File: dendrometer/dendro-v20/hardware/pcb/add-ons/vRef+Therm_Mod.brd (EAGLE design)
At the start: 10.2 x 15.7 mm, 9 parts, among them J1 MF-CON-2.54mm-01x03, J2 CON_01X01LUX, J4 MF-CON-2.54mm-01x03, U1 LM4040-SOT-23-3

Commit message: forgot to save
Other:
- board size 10.2 x 15.7 mm -> 8.9 x 15.2 mm
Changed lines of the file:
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@@
 <board>
 <plain>
-<wire x1="0" y1="0" x2="10.16" y2="0" width="0" layer="20"/>
-<wire x1="10.16" y1="0" x2="10.16" y2="15.24" width="0" layer="20"/>
-<wire x1="10.16" y1="15.24" x2="0" y2="15.24" width="0" layer="20"/>
+<wire x1="0" y1="0" x2="8.89" y2="0" width="0" layer="20"/>
+<wire x1="8.89" y1="0" x2="8.89" y2="15.24" width="0" layer="20"/>
+<wire x1="8.89" y1="15.24" x2="0" y2="15.24" width="0" layer="20"/>
 <wire x1="0" y1="15.24" x2="0" y2="0" width="0" layer="20"/>
 <wire x1="1.27" y1="0.635" x2="3.81" y2="0.635" width="0.3048" layer="46"/>
@@
 <wire x1="8.128" y1="3.429" x2="8.128" y2="5.842" width="0.3048" layer="46"/>
 <wire x1="8.128" y1="5.842" x2="8.763" y2="6.477" width="0.3048" layer="46"/>
-<wire x1="6.223" y1="13.208" x2="6.223" y2="15.621" width="0.3048" layer="46"/>
-<wire x1="1.397" y1="15.748" x2="1.397" y2="13.081" width="0.3048" layer="46"/>
 <wire x1="1.397" y1="13.081" x2="1.905" y2="12.827" width="0.3048" layer="46"/>
 <wire x1="1.905" y1="12.827" x2="2.921" y2="12.827" width="0.3048" layer="46"/>
@@
 <wire x1="7.112" y1="5.969" x2="8.001" y2="6.858" width="0.3048" layer="46"/>
 <wire x1="4.572" y1="12.319" x2="3.937" y2="12.954" width="0.3048" layer="46"/>
-<wire x1="3.937" y1="12.954" x2="3.937" y2="15.621" width="0.3048" layer="46"/>
 <wire x1="1.27" y1="0.635" x2="1.27" y2="2.159" width="0.3048" layer="46"/>
 <wire x1="1.27" y1="2.159" x2="2.032" y2="2.921" width="0.3048" layer="46"/>
@@
 <wire x1="6.858" y1="11.938" x2="6.477" y2="12.319" width="0.3048" layer="46"/>
 <wire x1="6.477" y1="12.319" x2="6.477" y2="12.954" width="0.3048" layer="46"/>
-<wire x1="6.477" y1="12.954" x2="6.223" y2="13.208" width="0.3048" layer="46"/>
+<wire x1="6.477" y1="12.954" x2="6.35" y2="13.081" width="0.3048" layer="46"/>
 <wire x1="4.191" y1="11.557" x2="5.207" y2="11.557" width="0.3048" layer="46"/>
 <wire x1="5.207" y1="11.557" x2="7.239" y2="9.525" width="0.3048" layer="46"/>
@@
 <wire x1="3.429" y1="2.921" x2="3.429" y2="4.699" width="0.3048" layer="46"/>
 <wire x1="3.429" y1="4.699" x2="3.937" y2="4.699" width="0.3048" layer="46"/>
+<wire x1="1.397" y1="13.081" x2="1.397" y2="14.605" width="0.3048" layer="46"/>
+<wire x1="1.397" y1="14.605" x2="3.937" y2="14.605" width="0.3048" layer="46"/>
+<wire x1="3.937" y1="14.605" x2="6.223" y2="14.605" width="0.3048" layer="46"/>
+<wire x1="6.223" y1="14.605" x2="6.35" y2="14.478" width="0.3048" layer="46"/>
+<wire x1="6.35" y1="14.478" x2="6.35" y2="13.081" width="0.3048" layer="46"/>
+<wire x1="3.937" y1="12.954" x2="3.937" y2="14.605" width="0.3048" layer="46"/>
 </plain>
 <attributes>

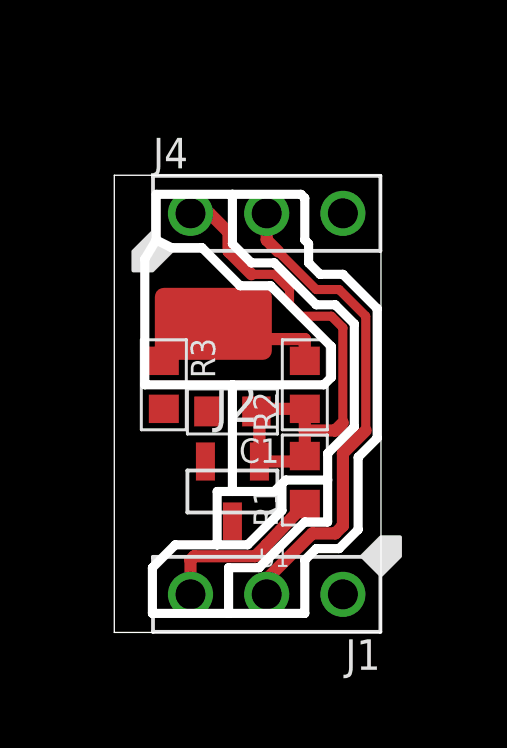
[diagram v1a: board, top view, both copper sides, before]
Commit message: making add-on boards for dendro upgrades)
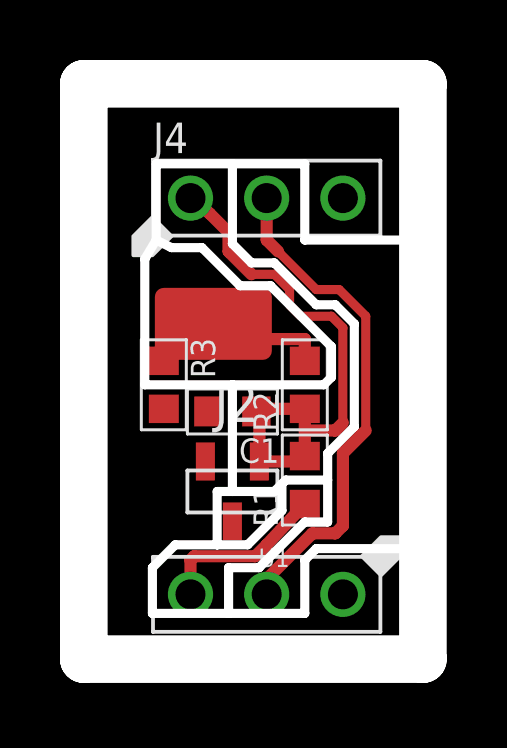
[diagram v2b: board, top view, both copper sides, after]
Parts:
- moved FRAME1 3.59 mm to (6.35, 19.1)
- moved J4 0.51 mm to (5.08, 14.5)
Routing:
- net SENSE: track 16.3 -> 16.8 mm
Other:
- board size 8.9 x 15.2 mm -> 11.3 x 19.2 mm
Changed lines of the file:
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@@
 <?xml version="1.0" encoding="utf-8"?>
 <!DOCTYPE eagle SYSTEM "eagle.dtd">
-<eagle version="8.0.0">
+<eagle version="8.0.1">
 <drawing>
 <settings>
@@
 <layer number="19" name="Unrouted" color="6" fill="1" visible="yes" active="yes"/>
 <layer number="20" name="Dimension" color="15" fill="1" visible="yes" active="yes"/>
-<layer number="21" name="tPlace" color="7" fill="1" visible="yes" active="yes"/>
-<layer number="22" name="bPlace" color="7" fill="1" visible="yes" active="yes"/>
+<layer number="21" name="tPlace" color="16" fill="1" visible="yes" active="yes"/>
+<layer number="22" name="bPlace" color="5" fill="1" visible="yes" active="yes"/>
 <layer number="23" name="tOrigins" color="15" fill="1" visible="yes" active="yes"/>
 <layer number="24" name="bOrigins" color="15" fill="1" visible="yes" active="yes"/>
@@
 <layer number="49" name="Reference" color="7" fill="1" visible="yes" active="yes"/>
 <layer number="50" name="dxf" color="7" fill="1" visible="no" active="no"/>
-<layer number="51" name="tDocu" color="7" fill="1" visible="yes" active="yes"/>
+<layer number="51" name="tDocu" color="6" fill="1" visible="yes" active="yes"/>
 <layer number="52" name="bDocu" color="7" fill="1" visible="no" active="yes"/>
 <layer number="53" name="tGND_GNDA" color="7" fill="9" visible="no" active="no"/>
@@
 <board>
 <plain>
-<wire x1="0" y1="0" x2="8.89" y2="0" width="0" layer="20"/>
-<wire x1="8.89" y1="0" x2="8.89" y2="15.24" width="0" layer="20"/>
-<wire x1="8.89" y1="15.24" x2="0" y2="15.24" width="0" layer="20"/>
-<wire x1="0" y1="15.24" x2="0" y2="0" width="0" layer="20"/>
+<wire x1="-1.016" y1="-0.889" x2="10.287" y2="-0.889" width="1.5875" layer="20"/>
+<wire x1="10.287" y1="-0.889" x2="10.287" y2="18.288" width="1.5875" layer="20"/>
+<wire x1="10.287" y1="18.288" x2="-1.016" y2="18.288" width="1.5875" layer="20"/>
+<wire x1="-1.016" y1="18.288" x2="-1.016" y2="-0.889" width="1.5875" layer="20"/>
 <wire x1="1.27" y1="0.635" x2="3.81" y2="0.635" width="0.3048" layer="46"/>
 <wire x1="3.81" y1="0.635" x2="6.35" y2="0.635" width="0.3048" layer="46"/>
 <wire x1="6.35" y1="0.635" x2="6.35" y2="2.413" width="0.3048" layer="46"/>
 <wire x1="6.35" y1="2.413" x2="6.731" y2="2.794" width="0.3048" layer="46"/>
-<wire x1="6.731" y1="2.794" x2="7.493" y2="2.794" width="0.3048" layer="46"/>
-<wire x1="7.493" y1="2.794" x2="8.128" y2="3.429" width="0.3048" layer="46"/>
-<wire x1="8.128" y1="3.429" x2="8.128" y2="5.842" width="0.3048" layer="46"/>
-<wire x1="8.128" y1="5.842" x2="8.763" y2="6.477" width="0.3048" layer="46"/>
+<wire x1="6.731" y1="2.794" x2="9.906" y2="2.794" width="0.3048" layer="46"/>
 <wire x1="1.397" y1="13.081" x2="1.905" y2="12.827" width="0.3048" layer="46"/>
 <wire x1="1.905" y1="12.827" x2="2.921" y2="12.827" width="0.3048" layer="46"/>
@@
 <wire x1="7.366" y1="10.922" x2="8.001" y2="10.287" width="0.3048" layer="46"/>
 <wire x1="8.001" y1="10.287" x2="8.001" y2="6.858" width="0.3048" layer="46"/>
-<wire x1="8.763" y1="6.477" x2="8.763" y2="10.795" width="0.3048" layer="46"/>
-<wire x1="8.763" y1="10.795" x2="7.62" y2="11.938" width="0.3048" layer="46"/>
-<wire x1="7.62" y1="11.938" x2="6.858" y2="11.938" width="0.3048" layer="46"/>
-<wire x1="6.858" y1="11.938" x2="6.477" y2="12.319" width="0.3048" layer="46"/>
-<wire x1="6.477" y1="12.319" x2="6.477" y2="12.954" width="0.3048" layer="46"/>
-<wire x1="6.477" y1="12.954" x2="6.35" y2="13.081" width="0.3048" layer="46"/>
+<wire x1="10.033" y1="13.081" x2="6.35" y2="13.081" width="0.3048" layer="46"/>
 <wire x1="4.191" y1="11.557" x2="5.207" y2="11.557" width="0.3048" layer="46"/>
 <wire x1="5.207" y1="11.557" x2="7.239" y2="9.525" width="0.3048" layer="46"/>
@@
 <wire x1="3.429" y1="2.921" x2="3.429" y2="4.699" width="0.3048" layer="46"/>
 <wire x1="3.429" y1="4.699" x2="3.937" y2="4.699" width="0.3048" layer="46"/>
-<wire x1="1.397" y1="13.081" x2="1.397" y2="14.605" width="0.3048" layer="46"/>
-<wire x1="1.397" y1="14.605" x2="3.937" y2="14.605" width="0.3048" layer="46"/>
-<wire x1="3.937" y1="14.605" x2="6.223" y2="14.605" width="0.3048" layer="46"/>
-<wire x1="6.223" y1="14.605" x2="6.35" y2="14.478" width="0.3048" layer="46"/>
-<wire x1="6.35" y1="14.478" x2="6.35" y2="13.081" width="0.3048" layer="46"/>
-<wire x1="3.937" y1="12.954" x2="3.937" y2="14.605" width="0.3048" layer="46"/>
+<wire x1="1.397" y1="13.081" x2="1.397" y2="15.621" width="0.3048" layer="46"/>
+<wire x1="1.397" y1="15.621" x2="3.937" y2="15.621" width="0.3048" layer="46"/>
+<wire x1="3.937" y1="15.621" x2="6.35" y2="15.621" width="0.3048" layer="46"/>
+<wire x1="6.35" y1="15.621" x2="6.35" y2="13.081" width="0.3048" layer="46"/>
+<wire x1="3.937" y1="12.954" x2="3.937" y2="15.621" width="0.3048" layer="46"/>
 </plain>
 <attributes>
@@
 <attribute name="PARTNO" value="" x="3.937" y="7.366" size="1.778" layer="27" rot="R180" display="off"/>
 </element>
-<element name="FRAME1" library="My_Aesthetics" package="DUMMY" value="FRAME-LETTERNO_PACKAGE" x="8.89" y="21.59">
-<attribute name="DESIGNER" value="Nobody" x="8.89" y="21.59" size="1.778" layer="27" display="off"/>
-<attribute name="VERSION" value="v01" x="8.89" y="21.59" size="1.778" layer="27" display="off"/>
-<attribute name="PARTNO" value="NA" x="8.89" y="21.59" size="1.778" layer="27" display="off"/>
+<element name="FRAME1" library="My_Aesthetics" package="DUMMY" value="FRAME-LETTERNO_PACKAGE" x="6.35" y="19.05">
+<attribute name="DESIGNER" value="Nobody" x="6.35" y="19.05" size="1.778" layer="27" display="off"/>
+<attribute name="VERSION" value="v01" x="6.35" y="19.05" size="1.778" layer="27" display="off"/>
+<attribute name="PARTNO" value="NA" x="6.35" y="19.05" size="1.778" layer="27" display="off"/>
 </element>
 <element name="J1" library="My_Connectors" package="PTH_2.54MM_01X03" value="MF-CON-2.54mm-01x03" x="5.08" y="1.27" rot="R180">
@@
 </element>
 <element name="J2" library="My_Connectors" package="1X01_LUXEON-PAD" value="CON_01X01LUX" x="3.302" y="10.287" rot="R180"/>
-<element name="J4" library="My_Connectors" package="PTH_2.54MM_01X03" value="MF-CON-2.54mm-01x03" x="5.08" y="13.97">
-<attribute name="MPN" value="MF-CON-2.54mm-01x03" x="5.08" y="13.97" size="1.778" layer="27" display="off"/>
-<attribute name="LABEL01" value="" x="5.08" y="13.97" size="1.778" layer="27" display="off"/>
-<attribute name="LABEL02" value="" x="5.08" y="13.97" size="1.778" layer="27" display="off"/>
-<attribute name="LABEL03" value="" x="5.08" y="13.97" size="1.778" layer="27" display="off"/>
-<attribute name="POPULATE" value="1" x="5.08" y="13.97" size="1.778" layer="27" display="off"/>
-<attribute name="PARTNO" value="" x="5.08" y="13.97" size="1.778" layer="27" display="off"/>
-<attribute name="HOUSEPART" value="YES" x="5.08" y="13.97" size="1.778" layer="27" display="off"/>
-<attribute name="URL" value="https://factory.macrofab.com/part/MF-CON-2.54mm-01x03" x="5.08" y="13.97" size="1.778" layer="27" display="off"/>
+<element name="J4" library="My_Connectors" package="PTH_2.54MM_01X03" value="MF-CON-2.54mm-01x03" x="5.08" y="14.478">
+<attribute name="MPN" value="MF-CON-2.54mm-01x03" x="5.08" y="14.478" size="1.778" layer="27" display="off"/>
+<attribute name="LABEL01" value="" x="5.08" y="14.478" size="1.778" layer="27" display="off"/>
+<attribute name="LABEL02" value="" x="5.08" y="14.478" size="1.778" layer="27" display="off"/>
+<attribute name="LABEL03" value="" x="5.08" y="14.478" size="1.778" layer="27" display="off"/>
+<attribute name="POPULATE" value="1" x="5.08" y="14.478" size="1.778" layer="27" display="off"/>
+<attribute name="PARTNO" value="" x="5.08" y="14.478" size="1.778" layer="27" display="off"/>
+<attribute name="HOUSEPART" value="YES" x="5.08" y="14.478" size="1.778" layer="27" display="off"/>
+<attribute name="URL" value="https://factory.macrofab.com/part/MF-CON-2.54mm-01x03" x="5.08" y="14.478" size="1.778" layer="27" display="off"/>
 </element>
 <element name="R1" library="My_Passives" package="R0603-N" value="100" x="6.35" y="5.08" rot="R90">
@@
 <contactref element="U1" pad="2"/>
 <contactref element="R3" pad="2"/>
-<wire x1="3.137" y1="7.366" x2="7.62" y2="13.97" width="0" layer="19" extent="1-1"/>
+<wire x1="3.137" y1="7.366" x2="7.62" y2="14.478" width="0" layer="19" extent="1-1"/>
 <wire x1="1.651" y1="7.455" x2="3.137" y2="7.366" width="0" layer="19" extent="1-1"/>
 <wire x1="3.037" y1="5.699" x2="3.137" y2="7.366" width="0" layer="19" extent="1-1"/>
@@
 <contactref element="J1" pad="P$2"/>
 <wire x1="5.08" y1="1.778" x2="5.08" y2="1.27" width="0.4064" layer="1"/>
-<wire x1="5.08" y1="13.97" x2="5.08" y2="13.081" width="0.4064" layer="1"/>
+<wire x1="5.08" y1="14.478" x2="5.08" y2="13.081" width="0.4064" layer="1"/>
 <wire x1="5.461" y1="12.7" x2="5.08" y2="13.081" width="0.4064" layer="1"/>
 <wire x1="7.62" y1="5.969" x2="8.382" y2="6.731" width="0.4064" layer="1"/>
@@
 <wire x1="7.366" y1="6.731" x2="7.62" y2="6.985" width="0.4064" layer="1"/>
 <wire x1="7.366" y1="6.731" x2="6.35" y2="6.731" width="0.4064" layer="1"/>
-<wire x1="2.54" y1="13.97" x2="3.175" y2="13.97" width="0.4064" layer="1"/>
+<wire x1="2.54" y1="14.478" x2="3.175" y2="13.97" width="0.4064" layer="1"/>
 <wire x1="3.175" y1="13.97" x2="3.81" y2="13.335" width="0.4064" layer="1"/>
 <wire x1="3.81" y1="13.335" x2="3.81" y2="12.7" width="0.4064" layer="1"/>
